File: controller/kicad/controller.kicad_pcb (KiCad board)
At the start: 2 copper layers, 90 x 88.4 mm, 27 parts, among them J1 pcie_98, U1 WeAct_STM32H750_Module, U10 ESD5344D, U11 ESD5344D, U12 ESD5344D, U13 ESD5344D, U14 ESD5344D, U15 ESD5344D, U16 ESD5344D, U17 ESD5344D, U18 ESD5344D, U19 ESD5344D, U2 ESD5344D, U20 ESD5344D, U21 ESD5344D, U3 ESD5344D, U4 ESD5344D, U5 ESD5344D, U6 ESD5344D, U7 ESD5344D, U8 ESD5344D, U9 ESD5344D

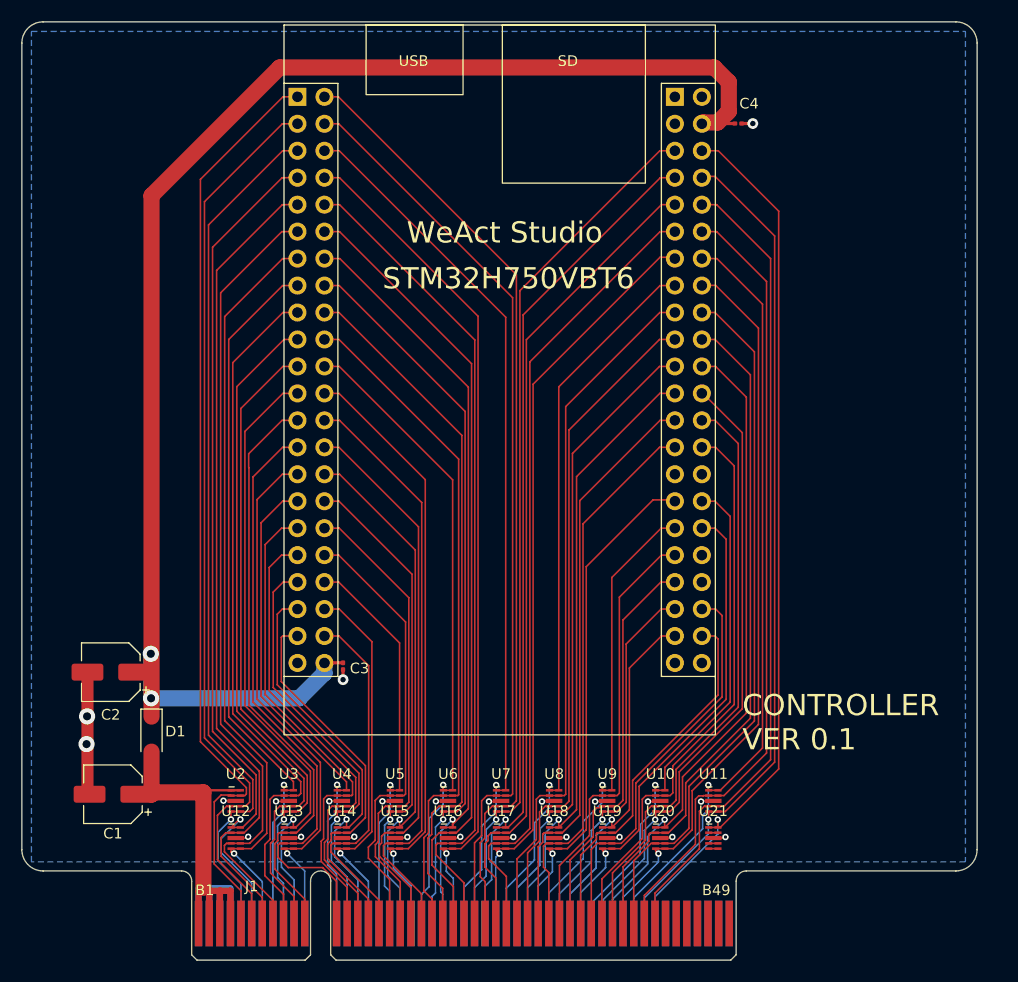
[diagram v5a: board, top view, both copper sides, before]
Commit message: Started to clean up unused controller signals.
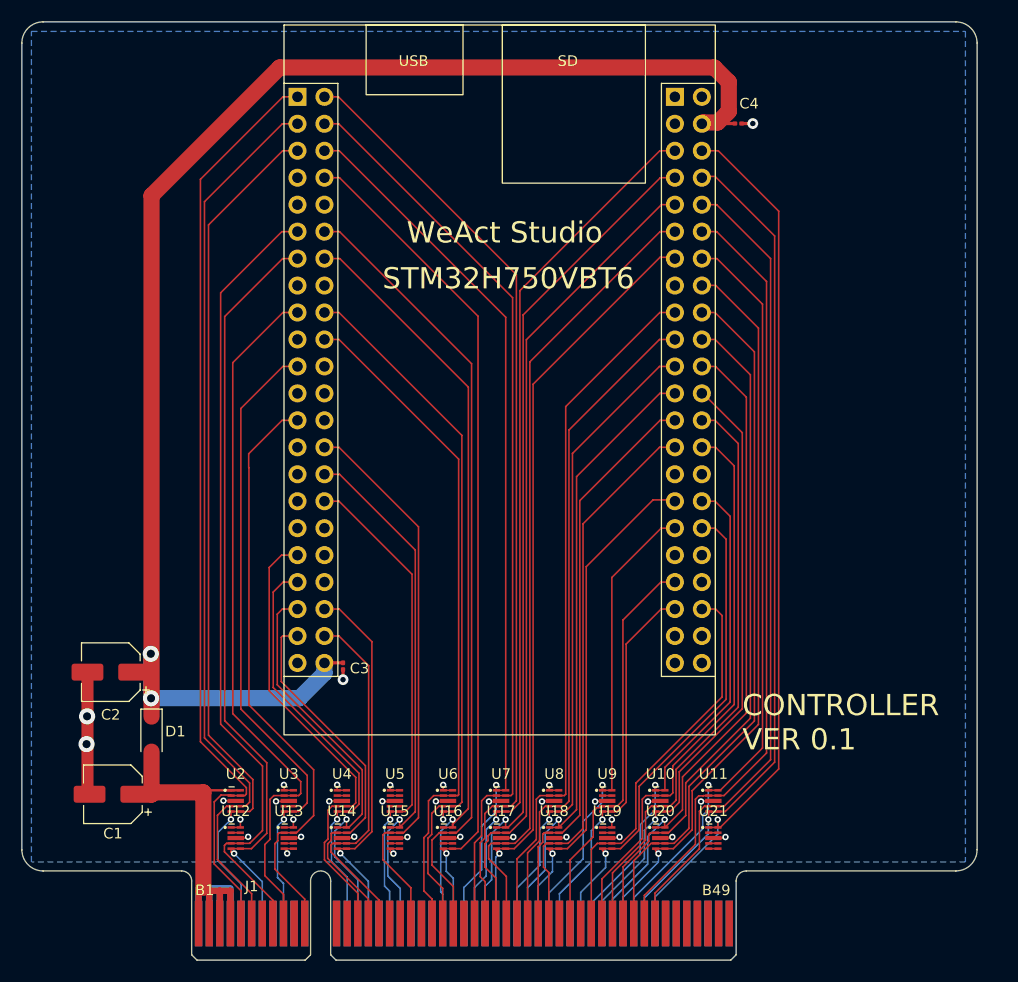
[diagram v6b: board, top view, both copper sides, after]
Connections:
- J1 pad A10: /PC11 -> unconnected-(J1-Pin_a10-PadA10)
- J1 pad A11: /PD4 -> unconnected-(J1-Pin_A11-PadA11)
- J1 pad A12: /PD6 -> unconnected-(J1-Pin_a12-PadA12)
- J1 pad A16: /PB6 -> unconnected-(J1-Pin_a16-PadA16)
- J1 pad A19: /PC10 -> unconnected-(J1-Pin_a19-PadA19)
- J1 pad A20: /PA12 -> unconnected-(J1-Pin_a20-PadA20)
- J1 pad A21: /PC8 -> unconnected-(J1-Pin_a21-PadA21)
- J1 pad A28: /PB2 -> unconnected-(J1-Pin_a28-PadA28)
- J1 pad A34: /PE2 -> unconnected-(J1-Pin_a34-PadA34)
- J1 pad A6: /PD11 -> unconnected-(J1-Pin_a6-PadA6)
- J1 pad A8: /PC9 -> unconnected-(J1-Pin_a8-PadA8)
- J1 pad B10: /PA11 -> unconnected-(J1-Pin_b10-PadB10)
- J1 pad B12: /PD2 -> unconnected-(J1-Pin_b12-PadB12)
- J1 pad B13: /PB3 -> unconnected-(J1-Pin_b13-PadB13)
- J1 pad B17: /PB4 -> unconnected-(J1-Pin_b17-PadB17)
- J1 pad B18: /PD7 -> unconnected-(J1-Pin_b18-PadB18)
- J1 pad B20: /PC12 -> unconnected-(J1-Pin_b20-PadB20)
- J1 pad B24: /PD12 -> unconnected-(J1-Pin_b24-PadB24)
- J1 pad B33: /PC13 -> unconnected-(J1-Pin_b33-PadB33)
- J1 pad B35: /PE3 -> unconnected-(J1-Pin_b35-PadB35)
- J1 pad B7: /PD13 -> unconnected-(J1-Pin_b7-PadB7)
- U1 pad 10: /PD12 -> unconnected-(U1A-PD12-Pad10)
- U1 pad 15: /PC9 -> unconnected-(U1A-PC9-Pad15)
- U1 pad 16: /PC8 -> unconnected-(U1A-PC8-Pad16)
- U1 pad 19: /PA11 -> unconnected-(U1A-PA11-Pad19)
- U1 pad 22: /PA12 -> unconnected-(U1A-PA12-Pad22)
- U1 pad 23: /PC11 -> unconnected-(U1A-PC11-Pad23)
- U1 pad 24: /PC10 -> unconnected-(U1A-PC10-Pad24)
- U1 pad 26: /PC12 -> unconnected-(U1A-PC12-Pad26)
- U1 pad 27: /PD2 -> unconnected-(U1A-PD2-Pad27)
- U1 pad 29: /PD4 -> unconnected-(U1A-PD4-Pad29)
- U1 pad 31: /PD6 -> unconnected-(U1A-PD6-Pad31)
- U1 pad 33: /PB3 -> unconnected-(U1A-PB3-Pad33)
- U1 pad 34: /PD7 -> unconnected-(U1A-PD7-Pad34)
- U1 pad 36: /PB4 -> unconnected-(U1A-PB4-Pad36)
- U1 pad 38: /PB6 -> unconnected-(U1A-PB6-Pad38)
- U1 pad 59: /PB2 -> unconnected-(U1B-PB2-Pad59)
- U1 pad 7: /PD11 -> unconnected-(U1A-PD11-Pad7)
- U1 pad 79: /PC13 -> unconnected-(U1B-PC13-Pad79)
- U1 pad 85: /PE2 -> unconnected-(U1B-PE2-Pad85)
- U1 pad 86: /PE3 -> unconnected-(U1B-PE3-Pad86)
- U1 pad 9: /PD13 -> unconnected-(U1A-PD13-Pad9)
- U12 pad 1: /PD11 -> unconnected-(U12-D1-Pad1)
- U12 pad 2: /PD13 -> unconnected-(U12-D2-Pad2)
- U13 pad 1: /PC11 -> unconnected-(U13-D1-Pad1)
- U13 pad 4: /PD2 -> unconnected-(U13-D3-Pad4)
- U13 pad 5: /PD4 -> unconnected-(U13-D4-Pad5)
- U15 pad 4: /PC12 -> unconnected-(U15-D3-Pad4)
- U15 pad 5: /PC10 -> unconnected-(U15-D4-Pad5)
- U16 pad 4: /PD12 -> unconnected-(U16-D3-Pad4)
- U19 pad 1: /PE2 -> unconnected-(U19-D1-Pad1)
- U19 pad 2: /PE3 -> unconnected-(U19-D2-Pad2)
- U3 pad 1: /PC9 -> unconnected-(U3-D1-Pad1)
- U3 pad 4: /PA11 -> unconnected-(U3-D3-Pad4)
- U4 pad 1: /PD6 -> unconnected-(U4-D1-Pad1)
- U4 pad 2: /PB3 -> unconnected-(U4-D2-Pad2)
- U5 pad 1: /PB6 -> unconnected-(U5-D1-Pad1)
- U5 pad 2: /PB4 -> unconnected-(U5-D2-Pad2)
- U5 pad 4: /PD7 -> unconnected-(U5-D3-Pad4)
- U6 pad 1: /PA12 -> unconnected-(U6-D1-Pad1)
- U6 pad 5: /PC8 -> unconnected-(U6-D4-Pad5)
- U8 pad 1: /PB2 -> unconnected-(U8-D1-Pad1)
- U9 pad 2: /PC13 -> unconnected-(U9-D2-Pad2)
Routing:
- net /PD11: track 81.5 -> 0.00 mm, vias 1 -> 0
- net /PD12: track 78.4 -> 0.00 mm
- net /PD13: track 77.5 -> 0.00 mm
- net /PB2: track 69.0 -> 0.00 mm, vias 1 -> 0
- net /PC8: track 68.5 -> 0.00 mm, vias 1 -> 0
- net /PC9: track 68.3 -> 0.00 mm, vias 1 -> 0
- net /PA11: track 64.5 -> 0.00 mm
- net /PA12: track 61.1 -> 0.00 mm, vias 1 -> 0
- net /PC11: track 59.5 -> 0.00 mm, vias 1 -> 0
- net /PC10: track 57.9 -> 0.00 mm, vias 1 -> 0
- net /PD2: track 56.9 -> 0.00 mm
- net /PC12: track 56.3 -> 0.00 mm
- net /PD4: track 50.4 -> 0.00 mm, vias 1 -> 0
- net /PD6: track 48.0 -> 0.00 mm, vias 1 -> 0
- net /PB3: track 46.4 -> 0.00 mm
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
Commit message: Removed unused TVS's and reassigned controller pins.
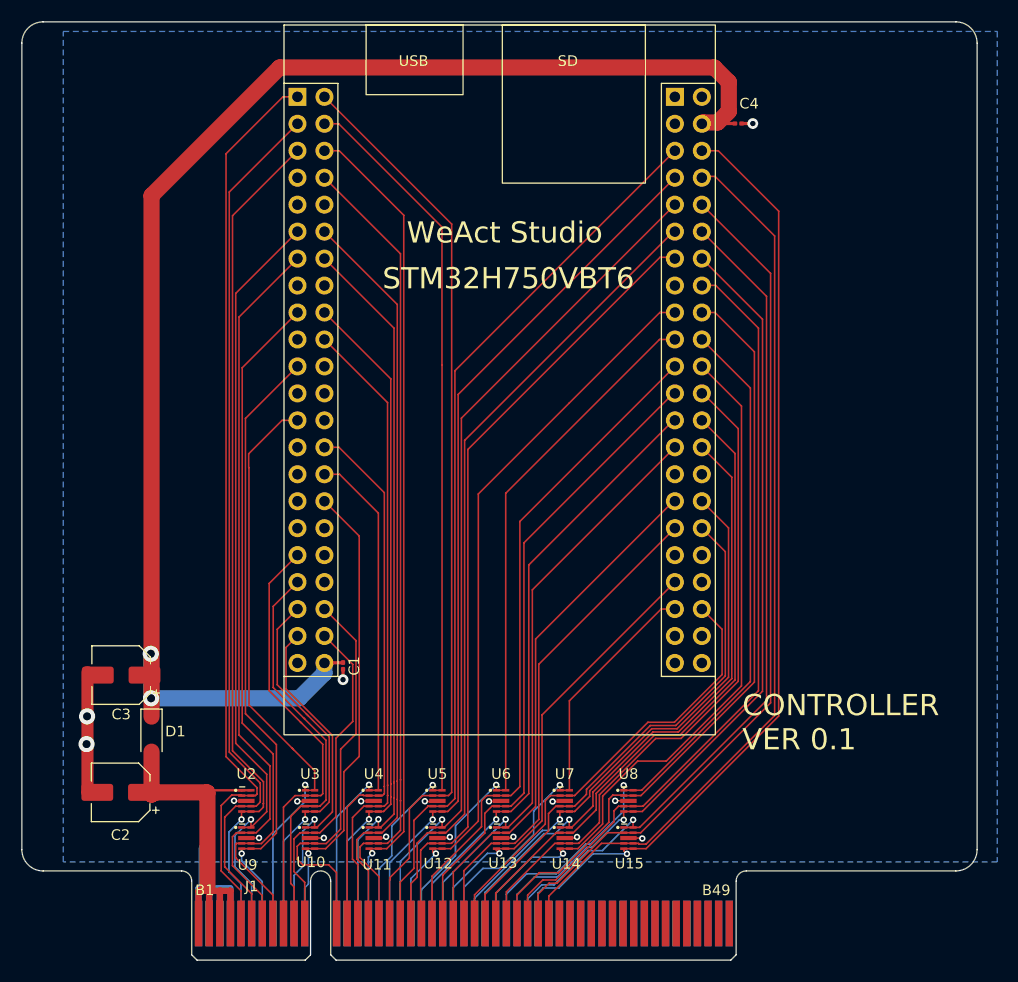
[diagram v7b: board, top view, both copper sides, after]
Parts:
- removed U16, U17, U18, U19, U20, U21: ESD5344D, common:Diodes_UDFN-10_1.0x2.5mm_P0.5mm
- C1: value 100uf -> 1uf; footprint controller:CP_Elec_5x5.4_JLCPCB -> Capacitor_SMD:C_0201_0603Metric
- C3: value 1uf -> 100uf; footprint Capacitor_SMD:C_0201_0603Metric -> controller:CP_Elec_5x5.4_JLCPCB
- moved U9 34.2 mm to (63.0, 48.5)
- moved U10 33.2 mm to (69.0, 48.5)
- moved U11 32.2 mm to (75.0, 48.5)
- moved C1 24.8 mm to (72.1, 32.3), turned to -90 degrees
- moved U15 22.0 mm to (99.0, 48.5)
- moved U14 21.0 mm to (93.0, 48.5)
- moved C3 20.9 mm to (51.2, 33.1), turned to 0 degrees
- moved U13 20.0 mm to (87.0, 48.5)
- moved U12 19.0 mm to (81.0, 48.5)
- moved C2 11.4 mm to (51.2, 44.2)
- moved U8 7.00 mm to (99.0, 45.0)
- moved U7 6.00 mm to (93.0, 45.0)
- moved U6 5.00 mm to (87.0, 45.0)
- moved U5 4.00 mm to (81.0, 45.0)
- moved U4 3.00 mm to (75.0, 45.0)
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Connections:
- C1 pad 1: /+5VBUS -> /+5V
- C2 pad 1: /+5V -> /+5VBUS
- J1 pad A10: unconnected-(J1-Pin_a10-PadA10) -> /PE1
- J1 pad A11: unconnected-(J1-Pin_A11-PadA11) -> /PD5
- J1 pad A12: unconnected-(J1-Pin_a12-PadA12) -> /PD3
- J1 pad A13: /PB7 -> /PA8
- J1 pad A14: /PB9 -> /PC6
- J1 pad A15: /PB8 -> /PD8
- J1 pad A16: unconnected-(J1-Pin_a16-PadA16) -> /PB14
- J1 pad A17: /PD5 -> /PE14
- J1 pad A18: /PD3 -> /PE12
- J1 pad A19: unconnected-(J1-Pin_a19-PadA19) -> /PB0
- J1 pad A20: unconnected-(J1-Pin_a20-PadA20) -> /PC4
- J1 pad A21: unconnected-(J1-Pin_a21-PadA21) -> /PA2
- J1 pad A22: /PC6 -> /PA0
- J1 pad A23: /PD10 -> /PE6
- J1 pad A24: /PD8 -> /PE4
- J1 pad A25: /PB10 -> /PC3
- J1 pad A26: /PE14 -> /PA1
- J1 pad A27: /PE8 -> /PA7
- J1 pad A28: unconnected-(J1-Pin_a28-PadA28) -> /PC5
- J1 pad A29: /PA6 -> /PE9
- J1 pad A30: /PA4 -> /PE11
- J1 pad A31: /PC2 -> /PB11
- J1 pad A32: /PC0 -> unconnected-(J1-Pin_a32-PadA32)
- J1 pad A33: /PE4 -> unconnected-(J1-Pin_a33-PadA33)
- J1 pad A35: /PC1 -> unconnected-(J1-Pin_a35-PadA35)
- J1 pad A36: /PC3 -> unconnected-(J1-Pin_a36-PadA36)
- J1 pad A37: /PA5 -> unconnected-(J1-Pin_a37-PadA37)
- J1 pad A38: /PA7 -> unconnected-(J1-Pin_a38-PadA38)
- J1 pad A39: /PE7 -> unconnected-(J1-Pin_a39-PadA39)
- J1 pad A40: /PE9 -> unconnected-(J1-Pin_a40-PadA40)
- J1 pad A41: /PE15 -> unconnected-(J1-Pin_a41-PadA41)
- J1 pad A42: /PB11 -> unconnected-(J1-Pin_a42-PadA42)
- J1 pad A6: unconnected-(J1-Pin_a6-PadA6) -> /PD15
- J1 pad A7: /PC7 -> /PA15
- J1 pad A8: unconnected-(J1-Pin_a8-PadA8) -> /PD0
- J1 pad A9: /PA15 -> /PB9
- J1 pad B10: unconnected-(J1-Pin_b10-PadB10) -> /PB7
- J1 pad B11: /PD0 -> /PE0
- J1 pad B12: unconnected-(J1-Pin_b12-PadB12) -> /PB8
- J1 pad B13: unconnected-(J1-Pin_b13-PadB13) -> /PD1
- J1 pad B14: /PB5 -> /PA10
- J1 pad B15: /PE1 -> /PD14
- J1 pad B16: /PE0 -> /PD10
- J1 pad B17: unconnected-(J1-Pin_b17-PadB17) -> /PB12
- J1 pad B18: unconnected-(J1-Pin_b18-PadB18) -> /PB10
- J1 pad B19: /PD1 -> /PE10
- J1 pad B20: unconnected-(J1-Pin_b20-PadB20) -> /PE8
- J1 pad B21: /PA10 -> /PA6
- J1 pad B22: /PA8 -> /PA4
- J1 pad B23: /PD14 -> /PC2
- J1 pad B24: unconnected-(J1-Pin_b24-PadB24) -> /PC0
- J1 pad B25: /PB14 -> /PE5
- J1 pad B26: /PB12 -> /PC1
- J1 pad B27: /PE12 -> /PA3
- J1 pad B28: /PE10 -> /PA5
- J1 pad B29: /PB0 -> /PB1
- J1 pad B30: /PC4 -> /PE7
- J1 pad B31: /PA2 -> /PE13
- J1 pad B32: /PA0 -> /PE15
- J1 pad B34: /PE6 -> unconnected-(J1-Pin_b34-PadB34)
- J1 pad B36: /PE5 -> unconnected-(J1-Pin_b36-PadB36)
- J1 pad B37: /PA1 -> unconnected-(J1-Pin_b37-PadB37)
- J1 pad B38: /PA3 -> unconnected-(J1-Pin_b38-PadB38)
- J1 pad B39: /PC5 -> unconnected-(J1-Pin_b39-PadB39)
- J1 pad B40: /PB1 -> unconnected-(J1-Pin_b40-PadB40)
- J1 pad B41: /PE11 -> unconnected-(J1-Pin_b41-PadB41)
- J1 pad B42: /PE13 -> unconnected-(J1-Pin_b42-PadB42)
- J1 pad B7: unconnected-(J1-Pin_b7-PadB7) -> /PC7
- J1 pad B8: /PD15 -> /PA9
- J1 pad B9: /PA9 -> /PB5
- U10 pad 1: /PC3 -> /PE1
- U10 pad 2: /PA1 -> /PE0
- U10 pad 4: /PA3 -> /PB8
- U10 pad 5: /PA5 -> /PD5
- U11 pad 1: /PE9 -> /PC6
- U11 pad 2: /PE11 -> /PD14
- U11 pad 4: /PE13 -> /PD10
- U11 pad 5: /PE15 -> /PD8
- U12 pad 1: unconnected-(U12-D1-Pad1) -> /PE12
- U12 pad 2: unconnected-(U12-D2-Pad2) -> /PE10
- U12 pad 4: /PD15 -> /PE8
- U12 pad 5: /PC7 -> /PB0
- U13 pad 1: unconnected-(U13-D1-Pad1) -> /PA0
- U13 pad 2: /PD0 -> /PC2
- U13 pad 4: unconnected-(U13-D3-Pad4) -> /PC0
- U13 pad 5: unconnected-(U13-D4-Pad5) -> /PE6
- U14 pad 1: /PB9 -> /PA1
- U14 pad 2: /PE1 -> /PA3
- U14 pad 4: /PE0 -> /PA5
- U14 pad 5: /PB8 -> /PA7
- U15 pad 1: /PD3 -> /PE11
- U15 pad 2: /PD1 -> /PE13
- U15 pad 4: unconnected-(U15-D3-Pad4) -> /PE15
- U15 pad 5: unconnected-(U15-D4-Pad5) -> /PB11
- U3 pad 1: unconnected-(U3-D1-Pad1) -> /PD0
- U3 pad 2: /PA9 -> /PB5
- U3 pad 4: unconnected-(U3-D3-Pad4) -> /PB7
- U3 pad 5: /PA15 -> /PB9
- U4 pad 1: unconnected-(U4-D1-Pad1) -> /PD3
- U4 pad 2: unconnected-(U4-D2-Pad2) -> /PD1
- U4 pad 4: /PB5 -> /PA10
- U4 pad 5: /PB7 -> /PA8
- U5 pad 1: unconnected-(U5-D1-Pad1) -> /PB14
- U5 pad 2: unconnected-(U5-D2-Pad2) -> /PB12
- U5 pad 4: unconnected-(U5-D3-Pad4) -> /PB10
- U5 pad 5: /PD5 -> /PE14
- U6 pad 1: unconnected-(U6-D1-Pad1) -> /PC4
- U6 pad 2: /PA10 -> /PA6
- U6 pad 4: /PA8 -> /PA4
- U6 pad 5: unconnected-(U6-D4-Pad5) -> /PA2
- U7 pad 1: /PD8 -> /PE4
- U7 pad 2: /PB14 -> /PE5
- U7 pad 4: /PB12 -> /PC1
- U7 pad 5: /PB10 -> /PC3
- U8 pad 1: unconnected-(U8-D1-Pad1) -> /PC5
- U8 pad 2: /PB0 -> /PB1
- U8 pad 4: /PC4 -> /PE7
- U8 pad 5: /PA6 -> /PE9
- U9 pad 1: /PC0 -> /PD15
- U9 pad 2: unconnected-(U9-D2-Pad2) -> /PC7
- U9 pad 4: /PE6 -> /PA9
- U9 pad 5: /PE4 -> /PA15
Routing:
- net GND: track 56.7 -> 49.7 mm, vias 24 -> 18
- net /PA1: track 53.4 -> 60.2 mm, vias 0 -> 1
- net /PC5: track 63.6 -> 70.3 mm, vias 0 -> 1
- net /PE11: track 74.7 -> 81.2 mm, vias 0 -> 1
- net /PB11: track 84.0 -> 90.3 mm
- net /PB1: track 66.3 -> 72.3 mm
- net /PA7: track 62.6 -> 67.9 mm
- net /PE15: track 80.0 -> 85.4 mm, vias 1 -> 0
- net /PE4: track 35.7 -> 41.1 mm
- net /PA5: track 57.9 -> 63.3 mm, vias 1 -> 0
- net /PE5: track 37.6 -> 42.9 mm
- net /PE13: track 76.8 -> 81.8 mm
- net /PE9: track 72.5 -> 77.4 mm
- net /PA3: track 55.5 -> 60.4 mm
- net /PC3: track 48.5 -> 53.3 mm
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
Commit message: Added to the controller USB/Serial data link.
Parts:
- added C5: 100n, Capacitor_SMD:C_0603_1608Metric, F.Cu at (47.3, -15.6)
- added C6: 1u, Capacitor_SMD:C_0603_1608Metric, F.Cu at (47.3, -13.9)
- added C7: 100n, Capacitor_SMD:C_0603_1608Metric, F.Cu at (47.3, -12.2)
- added C8: 4u7, Capacitor_SMD:C_0603_1608Metric, F.Cu at (47.3, -17.3)
- added J2: USB_C_Receptacle_USB2.0, controller:USB_C_Receptacle_XKB_U262-16XN-4BVC11, F.Cu at (53.7, -22.8)
- added JP1: Jumper_2_Open, Connector_PinHeader_2.54mm:PinHeader_1x02_P2.54mm_Vertical, F.Cu at (50.8, -4.91)
- added R1: 5K1, Resistor_SMD:R_0603_1608Metric, F.Cu at (57.2, -17.9)
- added R2: 5K1, Resistor_SMD:R_0603_1608Metric, F.Cu at (50.6, -18.0)
- added R3: 1K, Resistor_SMD:R_0603_1608Metric, F.Cu at (54.3, -4.29)
- added R4: 1K, Resistor_SMD:R_0603_1608Metric, F.Cu at (56.9, -4.22)
- added R5: 5K1, Resistor_SMD:R_0603_1608Metric, F.Cu at (47.3, -10.5)
- added U16: CP2102N-A01-GQFN28-Interface_USB, controller:QFN-28-1EP_5x5mm_P0.5mm_EP3.35x3.35mm, F.Cu at (53.5, -12.0)
- C1, C4: footprint Capacitor_SMD:C_0201_0603Metric -> Capacitor_SMD:C_0603_1608Metric
- moved C1 0.77 mm to (72.7, 32.8)
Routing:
- net /PB14: track 84.7 -> 120.8 mm, vias 1 -> 3
- net /PB15: track 82.8 -> 107.9 mm, vias 0 -> 2
- net Net-(J2-VBUS): track 0.00 -> 23.1 mm
- net GND: track 49.7 -> 65.7 mm, vias 18 -> 24
- net Net-(U16-VDD): track 0.00 -> 14.8 mm, vias 0 -> 2
- net Net-(U16-D+): track 0.00 -> 9.11 mm
- net Net-(U16-TXD): track 0.00 -> 8.71 mm
- net Net-(U16-RXD): track 0.00 -> 8.44 mm
- net Net-(U16-D-): track 0.00 -> 8.29 mm, vias 0 -> 2
- net Net-(U16-~{RSTb}): track 0.00 -> 4.83 mm
- net Net-(J2-CC1): track 0.00 -> 3.09 mm
- net Net-(J2-CC2): track 0.00 -> 2.65 mm
- net /PD0: track 56.1 -> 53.9 mm
- net /PE0: track 32.0 -> 33.5 mm
- net /PC7: track 69.9 -> 68.7 mm
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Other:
- board text added: "DATA LINK"
- board text added: "LOOP TEST"
